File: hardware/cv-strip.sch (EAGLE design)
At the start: 101 parts, among them IC1 PIC16F1825SO14, IC2 AD5696R, IC3 MC14094B, IC4 MC14094B, IC5 LM324D, IC6 REG1117, IC7 6N138

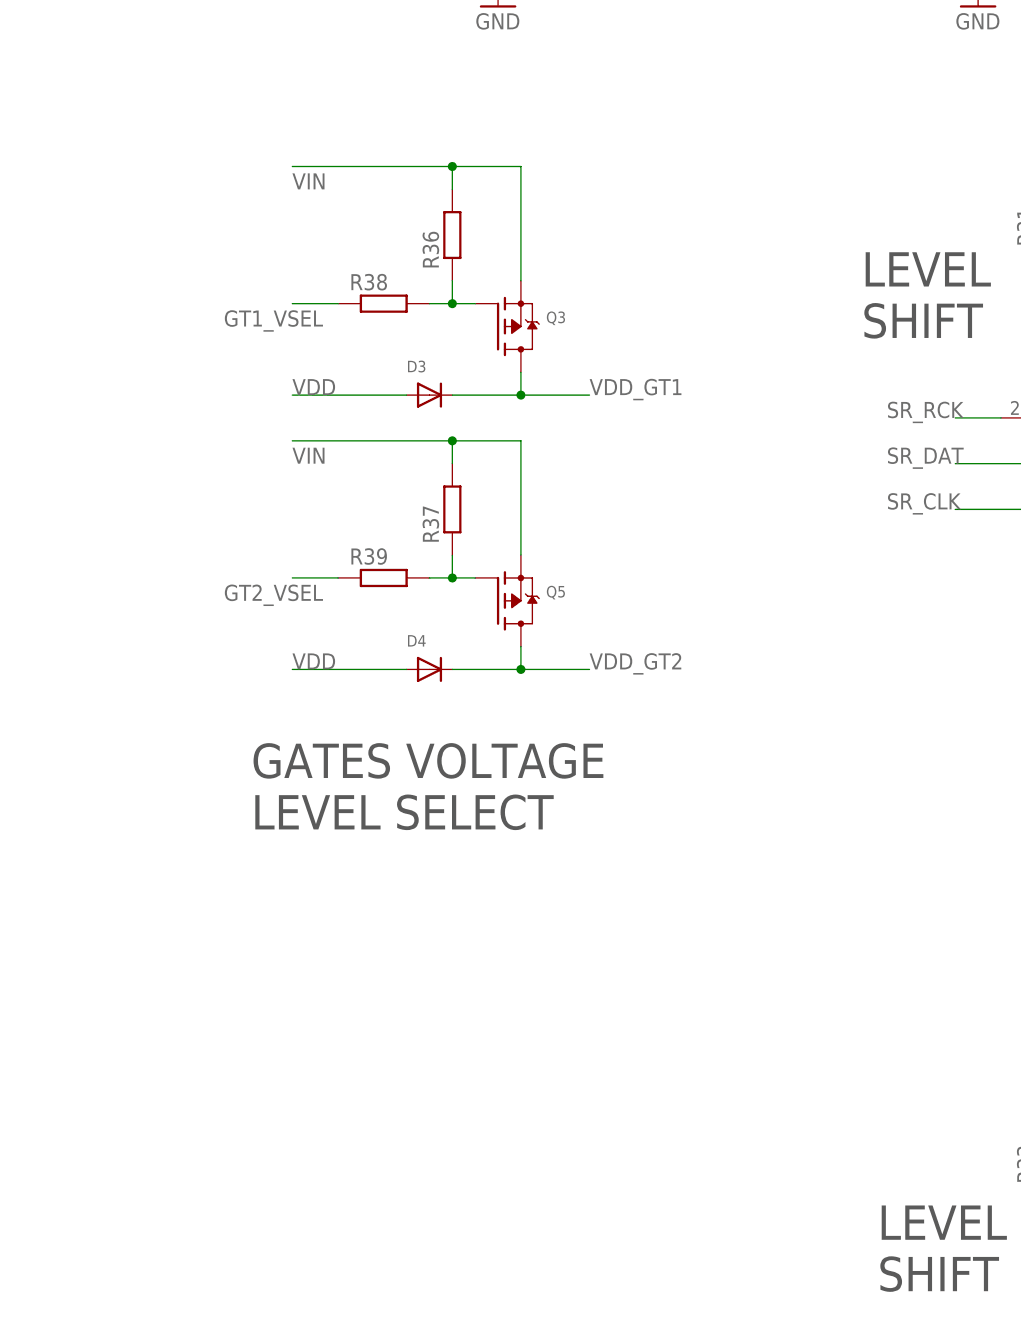
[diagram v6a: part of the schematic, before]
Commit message: extra n fet on voltage select circuits
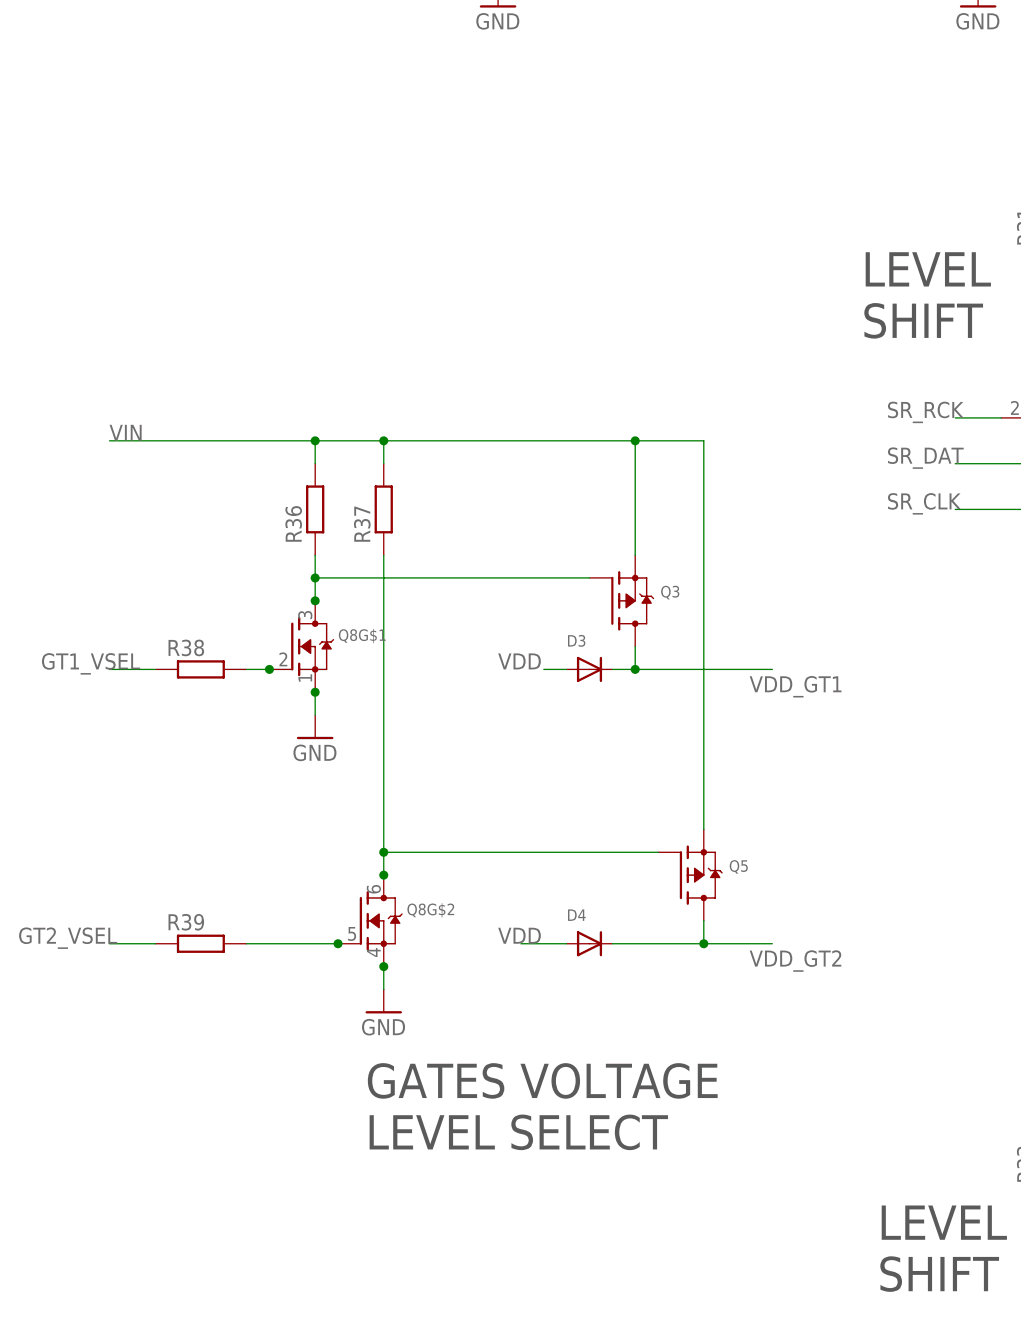
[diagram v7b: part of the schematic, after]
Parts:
- added Q8: (no value), microbuilder:MOSFET-N_DUAL
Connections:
- new net N$22: Q8G$1.G, R38.2
- new net N$47: Q8G$2.G, R39.2
- net GND: now also Q8G$1.S, Q8G$2.S
- net N$21: now also Q8G$2.D; no longer R39.2
- net N$9: now also Q8G$1.D; no longer R38.2
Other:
- moved on the sheet: D3, D4, Q3, Q5, R36, R37, R38, R39
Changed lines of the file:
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@@
 <part name="D5" library="microbuilder" deviceset="DIODE" device="SOD-123"/>
 <part name="C22" library="microbuilder" deviceset="CAP_TANTALUM" device="A/3216_REFLOW"/>
+<part name="GND9" library="supply1" deviceset="GND" device=""/>
+<part name="GND15" library="supply1" deviceset="GND" device=""/>
+<part name="Q8" library="microbuilder" deviceset="MOSFET-N_DUAL" device=""/>
 </parts>
 <sheets>
 <sheet>
 <plain>
-<text x="-121.412" y="-58.42" size="3.81" layer="97">GATES VOLTAGE
+<text x="-108.712" y="-93.98" size="3.81" layer="97">GATES VOLTAGE
 LEVEL SELECT</text>
 <text x="13.716" y="56.388" size="3.81" layer="97">CV OUTPUT
@@
 <instance part="Q2" gate="G$2" x="-20.32" y="-20.32"/>
 <instance part="Q4" gate="G$2" x="-20.32" y="-124.46"/>
-<instance part="R36" gate="G$1" x="-99.06" y="7.62" rot="R90"/>
-<instance part="R37" gate="G$1" x="-99.06" y="-22.86" rot="R90"/>
-<instance part="R38" gate="G$1" x="-106.68" y="0"/>
-<instance part="R39" gate="G$1" x="-106.68" y="-30.48"/>
-<instance part="Q3" gate="G$1" x="-91.44" y="-2.54"/>
-<instance part="D3" gate="G$1" x="-101.6" y="-10.16"/>
-<instance part="D4" gate="G$1" x="-101.6" y="-40.64"/>
-<instance part="Q5" gate="G$1" x="-91.44" y="-33.02"/>
+<instance part="R36" gate="G$1" x="-114.3" y="-22.86" rot="R90"/>
+<instance part="R37" gate="G$1" x="-106.68" y="-22.86" rot="R90"/>
+<instance part="R38" gate="G$1" x="-127" y="-40.64"/>
+<instance part="R39" gate="G$1" x="-127" y="-71.12"/>
+<instance part="Q3" gate="G$1" x="-78.74" y="-33.02"/>
+<instance part="D3" gate="G$1" x="-83.82" y="-40.64"/>
+<instance part="D4" gate="G$1" x="-83.82" y="-71.12"/>
+<instance part="Q5" gate="G$1" x="-71.12" y="-63.5"/>
 <instance part="D5" gate="G$1" x="-93.98" y="160.02"/>
 <instance part="C22" gate="G$1" x="63.5" y="66.04"/>
+<instance part="GND9" gate="1" x="-114.3" y="-48.26"/>
+<instance part="GND15" gate="1" x="-106.68" y="-78.74"/>
+<instance part="Q8" gate="G$1" x="-116.84" y="-38.1"/>
+<instance part="Q8" gate="G$2" x="-109.22" y="-68.58"/>
 </instances>
 <busses>
@@
 <wire x1="63.5" y1="60.96" x2="63.5" y2="63.5" width="0.1524" layer="91"/>
 </segment>
+<segment>
+<pinref part="GND9" gate="1" pin="GND"/>
+<wire x1="-114.3" y1="-43.18" x2="-114.3" y2="-45.72" width="0.1524" layer="91"/>
+<pinref part="Q8" gate="G$1" pin="S"/>
+<junction x="-114.3" y="-43.18"/>
+</segment>
+<segment>
+<pinref part="GND15" gate="1" pin="GND"/>
+<wire x1="-106.68" y1="-76.2" x2="-106.68" y2="-73.66" width="0.1524" layer="91"/>
+<pinref part="Q8" gate="G$2" pin="S"/>
+<junction x="-106.68" y="-73.66"/>
+</segment>
 </net>
 <net name="N$1" class="0">
@@
 <segment>
 <pinref part="D3" gate="G$1" pin="A"/>
-<wire x1="-104.14" y1="-10.16" x2="-116.84" y2="-10.16" width="0.1524" layer="91"/>
-<label x="-116.84" y="-10.16" size="1.778" layer="95"/>
+<wire x1="-86.36" y1="-40.64" x2="-88.9" y2="-40.64" width="0.1524" layer="91"/>
+<label x="-93.98" y="-40.64" size="1.778" layer="95"/>
 </segment>
 <segment>
 <pinref part="D4" gate="G$1" pin="A"/>
-<wire x1="-104.14" y1="-40.64" x2="-116.84" y2="-40.64" width="0.1524" layer="91"/>
-<label x="-116.84" y="-40.64" size="1.778" layer="95"/>
+<wire x1="-86.36" y1="-71.12" x2="-91.44" y2="-71.12" width="0.1524" layer="91"/>
+<label x="-93.98" y="-71.12" size="1.778" layer="95"/>
 </segment>
 </net>
@@
 </segment>
 <segment>
+<pinref part="Q5" gate="G$1" pin="S"/>
 <pinref part="Q3" gate="G$1" pin="S"/>
-<wire x1="-91.44" y1="2.54" x2="-91.44" y2="15.24" width="0.1524" layer="91"/>
-<wire x1="-91.44" y1="15.24" x2="-99.06" y2="15.24" width="0.1524" layer="91"/>
+<wire x1="-78.74" y1="-27.94" x2="-78.74" y2="-15.24" width="0.1524" layer="91"/>
+<wire x1="-78.74" y1="-15.24" x2="-106.68" y2="-15.24" width="0.1524" layer="91"/>
 <pinref part="R36" gate="G$1" pin="2"/>
-<wire x1="-99.06" y1="15.24" x2="-116.84" y2="15.24" width="0.1524" layer="91"/>
-<wire x1="-99.06" y1="12.7" x2="-99.06" y2="15.24" width="0.1524" layer="91"/>
-<junction x="-99.06" y="15.24"/>
-<label x="-116.84" y="12.7" size="1.778" layer="95"/>
-</segment>
-<segment>
-<pinref part="Q5" gate="G$1" pin="S"/>
-<wire x1="-116.84" y1="-15.24" x2="-99.06" y2="-15.24" width="0.1524" layer="91"/>
-<wire x1="-99.06" y1="-15.24" x2="-91.44" y2="-15.24" width="0.1524" layer="91"/>
-<wire x1="-91.44" y1="-15.24" x2="-91.44" y2="-27.94" width="0.1524" layer="91"/>
+<wire x1="-106.68" y1="-15.24" x2="-114.3" y2="-15.24" width="0.1524" layer="91"/>
+<wire x1="-114.3" y1="-15.24" x2="-137.16" y2="-15.24" width="0.1524" layer="91"/>
+<wire x1="-114.3" y1="-17.78" x2="-114.3" y2="-15.24" width="0.1524" layer="91"/>
+<junction x="-114.3" y="-15.24"/>
+<label x="-137.16" y="-15.24" size="1.778" layer="95"/>
+<wire x1="-78.74" y1="-15.24" x2="-71.12" y2="-15.24" width="0.1524" layer="91"/>
+<wire x1="-71.12" y1="-15.24" x2="-71.12" y2="-58.42" width="0.1524" layer="91"/>
+<junction x="-78.74" y="-15.24"/>
 <pinref part="R37" gate="G$1" pin="2"/>
-<wire x1="-99.06" y1="-17.78" x2="-99.06" y2="-15.24" width="0.1524" layer="91"/>
-<junction x="-99.06" y="-15.24"/>
-<label x="-116.84" y="-17.78" size="1.778" layer="95"/>
+<wire x1="-106.68" y1="-17.78" x2="-106.68" y2="-15.24" width="0.1524" layer="91"/>
+<junction x="-106.68" y="-15.24"/>
 </segment>
 </net>
@@
 <pinref part="D3" gate="G$1" pin="C"/>
 <pinref part="Q3" gate="G$1" pin="D"/>
-<wire x1="-99.06" y1="-10.16" x2="-91.44" y2="-10.16" width="0.1524" layer="91"/>
-<wire x1="-91.44" y1="-10.16" x2="-91.44" y2="-7.62" width="0.1524" layer="91"/>
-<wire x1="-91.44" y1="-10.16" x2="-83.82" y2="-10.16" width="0.1524" layer="91"/>
-<junction x="-91.44" y="-10.16"/>
-<label x="-83.82" y="-10.16" size="1.778" layer="95"/>
+<wire x1="-81.28" y1="-40.64" x2="-78.74" y2="-40.64" width="0.1524" layer="91"/>
+<wire x1="-78.74" y1="-40.64" x2="-78.74" y2="-38.1" width="0.1524" layer="91"/>
+<wire x1="-78.74" y1="-40.64" x2="-63.5" y2="-40.64" width="0.1524" layer="91"/>
+<junction x="-78.74" y="-40.64"/>
+<label x="-66.04" y="-43.18" size="1.778" layer="95"/>
 </segment>
 </net>
@@
 <pinref part="D4" gate="G$1" pin="C"/>
 <pinref part="Q5" gate="G$1" pin="D"/>
-<wire x1="-99.06" y1="-40.64" x2="-91.44" y2="-40.64" width="0.1524" layer="91"/>
-<wire x1="-91.44" y1="-40.64" x2="-91.44" y2="-38.1" width="0.1524" layer="91"/>
-<wire x1="-91.44" y1="-40.64" x2="-83.82" y2="-40.64" width="0.1524" layer="91"/>
-<junction x="-91.44" y="-40.64"/>
-<label x="-83.82" y="-40.64" size="1.778" layer="95"/>
+<wire x1="-81.28" y1="-71.12" x2="-71.12" y2="-71.12" width="0.1524" layer="91"/>
+<wire x1="-71.12" y1="-71.12" x2="-71.12" y2="-68.58" width="0.1524" layer="91"/>
+<wire x1="-71.12" y1="-71.12" x2="-63.5" y2="-71.12" width="0.1524" layer="91"/>
+<junction x="-71.12" y="-71.12"/>
+<label x="-66.04" y="-73.66" size="1.778" layer="95"/>
 </segment>
 </net>
@@
 <segment>
 <pinref part="R39" gate="G$1" pin="1"/>
-<wire x1="-111.76" y1="-30.48" x2="-116.84" y2="-30.48" width="0.1524" layer="91"/>
-<label x="-124.46" y="-33.02" size="1.778" layer="95"/>
+<wire x1="-132.08" y1="-71.12" x2="-137.16" y2="-71.12" width="0.1524" layer="91"/>
+<label x="-147.32" y="-71.12" size="1.778" layer="95"/>
 </segment>
 <segment>
@@
 <segment>
 <pinref part="R38" gate="G$1" pin="1"/>
-<wire x1="-111.76" y1="0" x2="-116.84" y2="0" width="0.1524" layer="91"/>
-<label x="-124.46" y="-2.54" size="1.778" layer="95"/>
+<wire x1="-132.08" y1="-40.64" x2="-137.16" y2="-40.64" width="0.1524" layer="91"/>
+<label x="-144.78" y="-40.64" size="1.778" layer="95"/>
 </segment>
 <segment>
@@
 <net name="N$9" class="0">
 <segment>
+<pinref part="Q3" gate="G$1" pin="G"/>
+<pinref part="R36" gate="G$1" pin="1"/>
+<wire x1="-114.3" y1="-30.48" x2="-83.82" y2="-30.48" width="0.1524" layer="91"/>
+<wire x1="-114.3" y1="-27.94" x2="-114.3" y2="-30.48" width="0.1524" layer="91"/>
+<wire x1="-114.3" y1="-30.48" x2="-114.3" y2="-33.02" width="0.1524" layer="91"/>
+<junction x="-114.3" y="-30.48"/>
+<pinref part="Q8" gate="G$1" pin="D"/>
+<junction x="-114.3" y="-33.02"/>
+</segment>
+</net>
+<net name="N$21" class="0">
+<segment>
+<pinref part="Q5" gate="G$1" pin="G"/>
+<pinref part="R37" gate="G$1" pin="1"/>
+<wire x1="-106.68" y1="-60.96" x2="-76.2" y2="-60.96" width="0.1524" layer="91"/>
+<wire x1="-106.68" y1="-27.94" x2="-106.68" y2="-60.96" width="0.1524" layer="91"/>
+<wire x1="-106.68" y1="-63.5" x2="-106.68" y2="-60.96" width="0.1524" layer="91"/>
+<junction x="-106.68" y="-60.96"/>
+<pinref part="Q8" gate="G$2" pin="D"/>
+<junction x="-106.68" y="-63.5"/>
+</segment>
+</net>
+<net name="N$22" class="0">
+<segment>
 <pinref part="R38" gate="G$1" pin="2"/>
-<pinref part="Q3" gate="G$1" pin="G"/>
-<wire x1="-101.6" y1="0" x2="-99.06" y2="0" width="0.1524" layer="91"/>
-<pinref part="R36" gate="G$1" pin="1"/>
-<wire x1="-99.06" y1="0" x2="-96.52" y2="0" width="0.1524" layer="91"/>
-<wire x1="-99.06" y1="2.54" x2="-99.06" y2="0" width="0.1524" layer="91"/>
-<junction x="-99.06" y="0"/>
-</segment>
-</net>
-<net name="N$21" class="0">
+<wire x1="-121.92" y1="-40.64" x2="-119.38" y2="-40.64" width="0.1524" layer="91"/>
+<pinref part="Q8" gate="G$1" pin="G"/>
+<junction x="-119.38" y="-40.64"/>
+</segment>
+</net>
+<net name="N$47" class="0">
 <segment>
 <pinref part="R39" gate="G$1" pin="2"/>
-<pinref part="Q5" gate="G$1" pin="G"/>
-<wire x1="-101.6" y1="-30.48" x2="-99.06" y2="-30.48" width="0.1524" layer="91"/>
-<pinref part="R37" gate="G$1" pin="1"/>
-<wire x1="-99.06" y1="-30.48" x2="-96.52" y2="-30.48" width="0.1524" layer="91"/>
-<wire x1="-99.06" y1="-27.94" x2="-99.06" y2="-30.48" width="0.1524" layer="91"/>
-<junction x="-99.06" y="-30.48"/>
-</segment>
-</net>
+<wire x1="-121.92" y1="-71.12" x2="-111.76" y2="-71.12" width="0.1524" layer="91"/>
+<pinref part="Q8" gate="G$2" pin="G"/>
+<junction x="-111.76" y="-71.12"/>
+</segment>
+</net>

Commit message: PCBrev2
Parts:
- added Q10, Q12, Q14: (no value), transistor:MMBT3904LT1-NPN-SOT23-BEC
- added Q11, Q13, Q7, Q9: (no value), microbuilder:MOSFET-P
- added Q6: (no value), microbuilder:MOSFET-N_DUAL
- added R40, R41, R42, R43, R44, R45, R46, R47: (no value), rcl:R-EU_R0805
- C10, C14, C15: value (none) -> 100n
- C16: device rcl:C-EUC0805 -> microbuilder:CAP_TANTALUMA/3216_REFLOW
- C18, C19, C9: value 100n -> (none)
- C20: device resistor:CPOL-EUE2.5-5 -> rcl:C-EUC0805
- C22: device microbuilder:CAP_TANTALUMA/3216_REFLOW -> resistor:CPOL-EUE2.5-5
- Q1, Q2: device microbuilder:MOSFET-N_DUAL -> microbuilder:MOSFET-P
- Q3, Q5: device microbuilder:MOSFET-P -> microbuilder:MOSFET-N_DUAL
- Q8: device microbuilder:MOSFET-N_DUAL -> transistor:MMBT3904LT1-NPN-SOT23-BEC
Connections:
- new net GT1: C18.1, GT1.4, R40.1, R47.2
- new net GT1H: IC3.Q4, Q9.G
- new net GT1L: IC3.Q8, R13.2
- new net GT2: C17.1, GT2.4, R41.1, R44.2
- new net GT2H: IC3.Q1, Q7.G
- new net GT2L: IC3.Q5, R14.2
- new net GT3: C20.1, GT3.4, R42.1, R45.2
- new net GT3H: IC3.Q3, Q13.G
- new net GT3L: IC3.Q7, R15.2
- new net GT4: C19.1, GT4.4, R43.1, R46.2
- new net GT4H: IC3.Q2, Q11.G
- new net GT4L: IC3.Q6, R16.2
- new net N$51: Q14.C, R45.1
- new net N$53: Q9.D, R40.2
- new net N$54: Q12.C, R46.1
- new net N$55: Q10.C, R47.1
- net GND: now also C10.2, C15.1, C16.-, C19.2, C20.2, C9.1, Q10.E, Q12.E, Q14.E, Q3G$1.S, Q3G$2.S, Q5G$1.S, Q5G$2.S, Q6G$1.S, Q6G$2.S, Q8.E; no longer C10.1, C15.2, C16.2, C19.1, C20.-, C9.2, Q1G$1.S, Q1G$2.S, Q2G$1.S, Q2G$2.S, Q8G$1.S, Q8G$2.S
- net N$1: now also Q7.D, R41.2; no longer C16.1, GT4.4, R15.2
- net N$10: now also Q8.B, R14.1; no longer IC3.Q2, R15.1
- net N$11: now also Q14.B, R15.1; no longer IC3.Q4, R16.1
- net N$12: now also Q12.B, R16.1; no longer IC3.Q3, R14.1
- net N$13: now also Q8.C, R44.1; no longer IC3.Q1, R13.1
- net N$14: now also Q6G$1.D; no longer Q1G$1.D
- net N$15: now also Q6G$2.D; no longer Q1G$2.D
- net N$16: now also Q5G$2.D; no longer Q2G$2.D
- net N$20: now also C8.1; no longer C4.1
- net N$21: now also Q2.G, Q3G$2.D; no longer Q5.G, Q8G$2.D
- net N$22: now also Q3G$1.G; no longer Q8G$1.G
- net N$23: now also C7.1; no longer C3.1
- net N$24: now also C6.1; no longer C2.1
- net N$33: now also C4.1; no longer C8.1
- net N$39: now also C3.1; no longer C7.1
- net N$41: now also C2.1; no longer C6.1
- net N$47: now also Q3G$2.G; no longer Q8G$2.G
- net N$48: now also Q5G$1.D; no longer Q2G$1.D
- net N$6: now also Q13.D, R42.2; no longer C17.1, GT3.4, R16.2
- net N$7: now also Q11.D, R43.2; no longer C15.1, GT1.4, R14.2
- net N$8: now also Q10.B, R13.1; no longer C14.1, GT2.4, R13.2
- net N$9: now also Q1.G, Q3G$1.D; no longer Q3.G, Q8G$1.D
- net SR_CLK: now also Q5G$2.G; no longer Q2G$2.G
- net SR_DAT: now also Q6G$2.G; no longer Q1G$2.G
- net SR_RCK: now also Q5G$1.G, Q6G$1.G; no longer Q1G$1.G, Q2G$1.G
- net VDD: now also C10.1, C15.2, C16.+, C21.+, C9.2; no longer C11.2, C19.2, C20.+, C22.+, C9.1
- net VDD_GT1: now also Q1.D, Q11.S, Q13.S, Q7.S, Q9.S; no longer Q3.D
- net VDD_GT2: now also Q2.D; no longer Q5.D
- net VIN: now also C11.2, C14.1, C22.+, Q1.S, Q2.S; no longer C10.2, C18.1, C21.+, Q3.S, Q5.S
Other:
- note added: "MIDI-TO-CV CONVERTER JASON HOTCHKISS SIXTY FOUR PIXELS LTD 13 JUN16"
- note removed: "MIDI-TO-CV CONVERTER JASON HOTCHKISS SIXTY FOUR PIXELS LTD 29 MAY 2016"
- moved on the sheet: C10, C11, C13, C14, C15, C17, C18, C19, C2, C21, C3, C4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
